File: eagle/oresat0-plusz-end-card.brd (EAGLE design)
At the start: 99.8 x 94.6 mm, 36 parts, among them J1 Harwin M55-7101242R, J10 R107064070_CONTACT, J11 R107064070_CONTACT, J12 R107064070_CONTACT, J13 R107064070_CONTACT, J14 R107064070_CONTACT, J15 R107064070_CONTACT, J16 R107064070_CONTACT, J2 Harwin M55-7101242R, J3 Harwin M55-7101242R, J4 Harwin M55-7101242R, J6 J-SAMTEC-TFM-120-X1-XXX-D-RA, J7 R107064070_CONTACT, J8 R107064070_CONTACT, J9 R107064070_CONTACT, U1 QCN-19D+, U2 QCN-19D+, U3 QCN-19D+

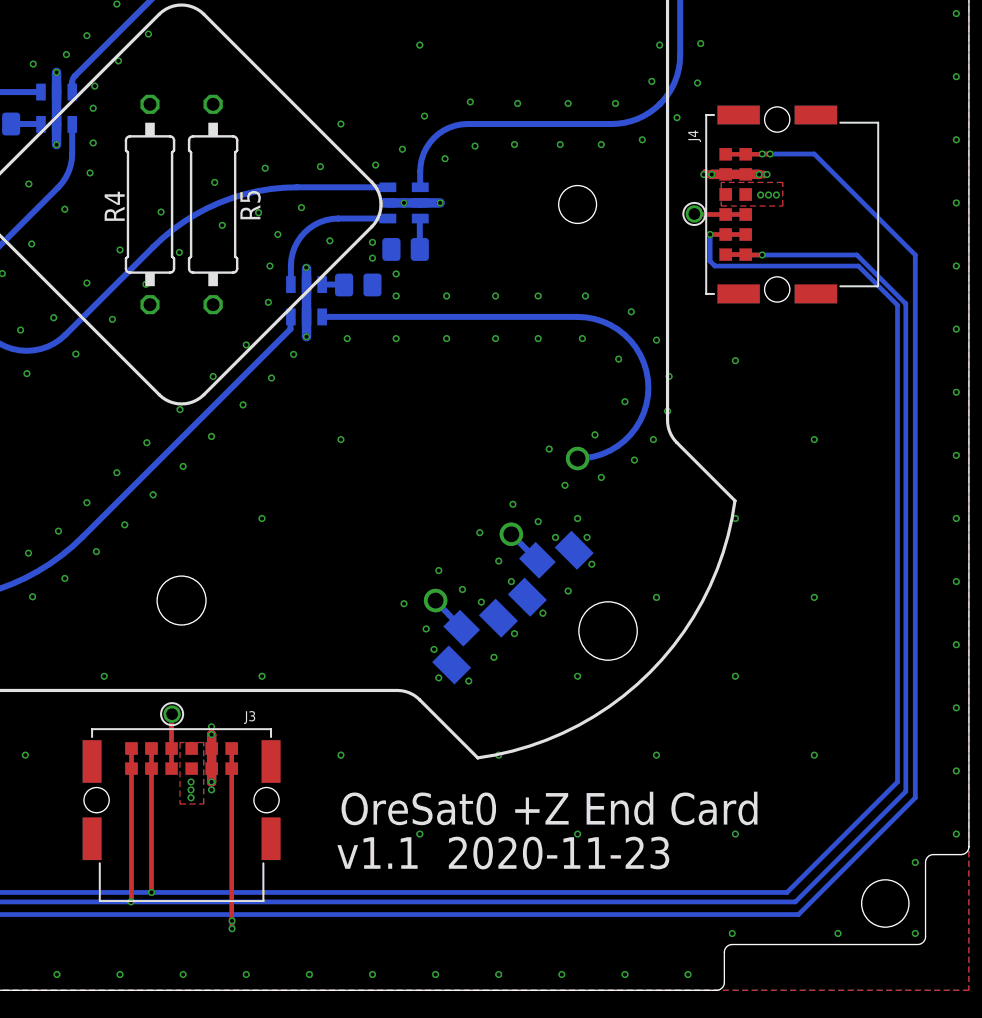
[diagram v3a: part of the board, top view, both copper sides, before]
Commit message: Small tweaks; reduced mezanine board size. Added flight tags. Off to fab!
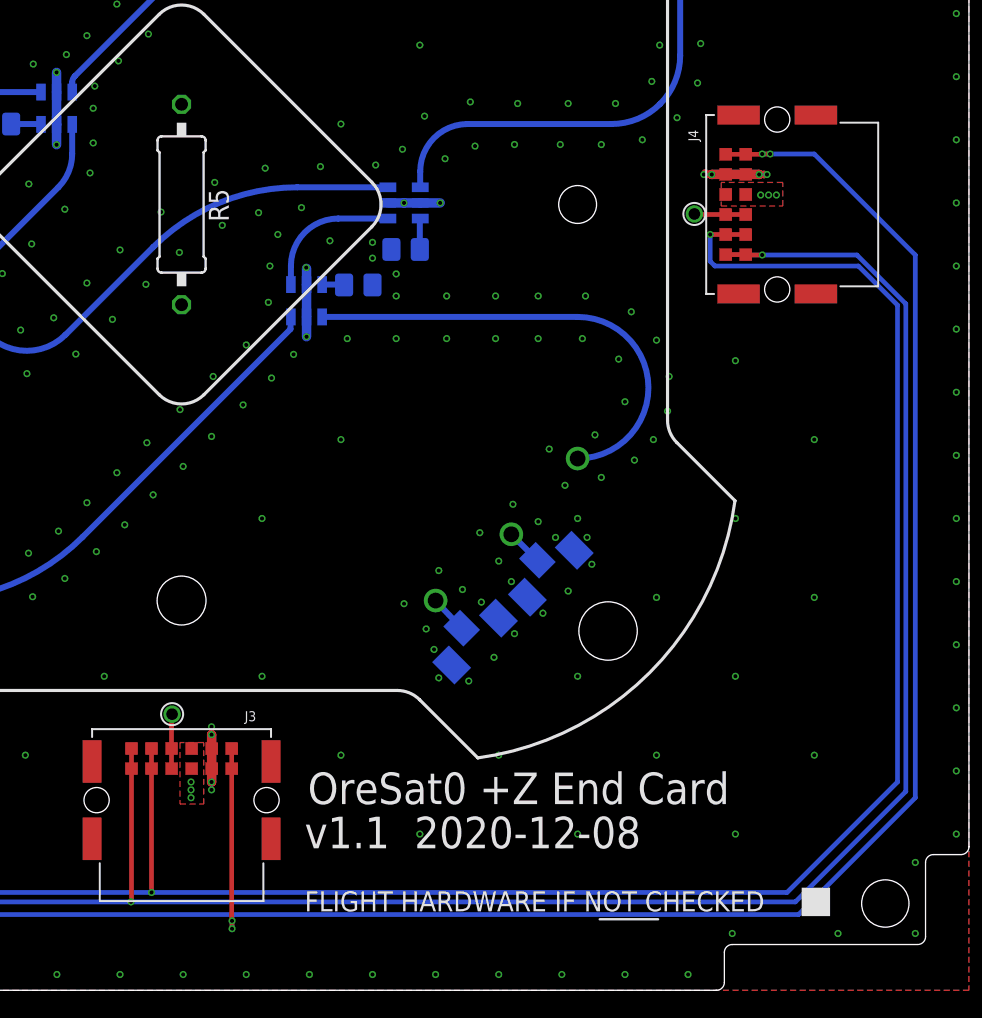
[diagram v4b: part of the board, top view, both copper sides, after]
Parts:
- removed R4: 1 1W, oresat-rcl:0309/12
- added U$1: FLIGHMARKERNEW, oresat-flight-marker:FLIGHTMARKER_NEW_BOARDS
- moved R5 2.00 mm to (49.9, 49.8)
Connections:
- net GND: no longer R4.1
- net TURNSTILE-DEPLOY: no longer R4.2
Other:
- board text added: "v1.1 2020-12-08"
- board text removed: "v1.1 2020-11-23"
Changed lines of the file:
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@@
 <layer number="14" name="Route14" color="22" fill="1" visible="no" active="no"/>
 <layer number="15" name="Route15" color="23" fill="1" visible="no" active="yes"/>
-<layer number="16" name="Bottom" color="1" fill="1" visible="no" active="yes"/>
+<layer number="16" name="Bottom" color="1" fill="1" visible="yes" active="yes"/>
 <layer number="17" name="Pads" color="2" fill="1" visible="yes" active="yes"/>
 <layer number="18" name="Vias" color="2" fill="1" visible="yes" active="yes"/>
@@
 <layer number="20" name="Dimension" color="24" fill="1" visible="yes" active="yes"/>
 <layer number="21" name="tPlace" color="7" fill="1" visible="yes" active="yes"/>
-<layer number="22" name="bPlace" color="7" fill="1" visible="no" active="yes"/>
+<layer number="22" name="bPlace" color="7" fill="1" visible="yes" active="yes"/>
 <layer number="23" name="tOrigins" color="15" fill="1" visible="yes" active="yes"/>
-<layer number="24" name="bOrigins" color="15" fill="1" visible="no" active="yes"/>
+<layer number="24" name="bOrigins" color="15" fill="1" visible="yes" active="yes"/>
 <layer number="25" name="tNames" color="7" fill="1" visible="yes" active="yes"/>
-<layer number="26" name="bNames" color="7" fill="1" visible="no" active="yes"/>
+<layer number="26" name="bNames" color="7" fill="1" visible="yes" active="yes"/>
 <layer number="27" name="tValues" color="7" fill="1" visible="no" active="yes"/>
 <layer number="28" name="bValues" color="7" fill="1" visible="no" active="yes"/>
 <layer number="29" name="tStop" color="7" fill="3" visible="yes" active="yes"/>
-<layer number="30" name="bStop" color="7" fill="6" visible="no" active="yes"/>
+<layer number="30" name="bStop" color="7" fill="6" visible="yes" active="yes"/>
 <layer number="31" name="tCream" color="7" fill="4" visible="no" active="yes"/>
 <layer number="32" name="bCream" color="7" fill="5" visible="no" active="yes"/>
@@
 <wire x1="60.01" y1="42.675" x2="75" y2="42.675" width="1.18" layer="30"/>
 <wire x1="75" y1="42.675" x2="76.5" y2="34" width="1.18" layer="30" curve="-159"/>
-<text x="59.9" y="10.5" size="2" layer="21" font="vector" ratio="10">OreSat0 +Z End Card</text>
-<text x="59.7" y="7.7" size="2" layer="21" font="vector" ratio="10">v1.1  2020-11-23</text>
+<text x="57.9" y="11.8" size="2" layer="21" font="vector" ratio="10">OreSat0 +Z End Card</text>
+<text x="57.7" y="9" size="2" layer="21" font="vector" ratio="10">v1.1  2020-12-08</text>
 <hole x="49.9" y="74.9" drill="3.1"/>
 <circle x="49.9" y="74.9" radius="3" width="0" layer="42"/>
@@
 <attribute name="VALUE" x="36.7" y="56.7" size="0.8" layer="28" font="vector" ratio="15" rot="MR180"/>
 </element>
-<element name="R4" library="oresat-rcl" package="0309/12" value="1 1W" x="47.9" y="49.8" smashed="yes" rot="R90">
-<attribute name="NAME" x="46.295003125" y="48.609" size="1.27" layer="25" ratio="10" rot="R90"/>
-<attribute name="VALUE" x="48.585803125" y="46.625" size="1.27" layer="27" ratio="10" rot="R90"/>
-</element>
-<element name="R5" library="oresat-rcl" package="0309/12" value="1 1W" x="51.9" y="49.8" smashed="yes" rot="R90">
-<attribute name="NAME" x="54.894996875" y="48.709" size="1.27" layer="25" ratio="10" rot="R90"/>
-<attribute name="VALUE" x="52.5858" y="46.625" size="1.27" layer="27" ratio="10" rot="R90"/>
+<element name="R5" library="oresat-rcl" package="0309/12" value="1 1W" x="49.9" y="49.8" locked="yes" smashed="yes" rot="R90">
+<attribute name="NAME" x="52.894996875" y="48.709" locked="yes" size="1.27" layer="25" ratio="10" rot="R90"/>
+<attribute name="VALUE" x="50.5858" y="46.625" locked="yes" size="1.27" layer="27" ratio="10" rot="R90"/>
 </element>
 <element name="J7" library="J-Radiall-R107064070-RF" package="R107064070_CONTACT" value="R107064070_CONTACT" x="88" y="75.9" locked="yes" smashed="yes" rot="MR90">
@@
 <attribute name="VALUE" x="68.5" y="19.271571875" locked="yes" size="0.655" layer="28" font="vector" ratio="20" rot="MR135"/>
 </element>
+<element name="U$1" library="oresat-flight-marker" package="FLIGHTMARKER_NEW_BOARDS" value="FLIGHMARKERNEW" x="57.7" y="5" smashed="yes"/>
 </elements>
 <signals>
@@
 <via x="30" y="44.9" extent="1-16" drill="0.254"/>
 <via x="65" y="89.9" extent="1-16" drill="0.254"/>
-<contactref element="R4" pad="1"/>
 <contactref element="R5" pad="1"/>
 <contactref element="J7" pad="P$3"/>
@@
 <contactref element="J6" pad="10"/>
 <contactref element="R5" pad="2"/>
-<contactref element="R4" pad="2"/>
 <polygon width="0.127" layer="2" isolate="0.2" thermals="no">
 <vertex x="33.8" y="90.5"/>
 <vertex x="33.8" y="54.5"/>
-<vertex x="54.4" y="54.5"/>
-<vertex x="54.4" y="65.2"/>
+<vertex x="51.6" y="54.5"/>
+<vertex x="51.6" y="68"/>
 <vertex x="42.5" y="77.1"/>
 <vertex x="42.5" y="90.5"/>

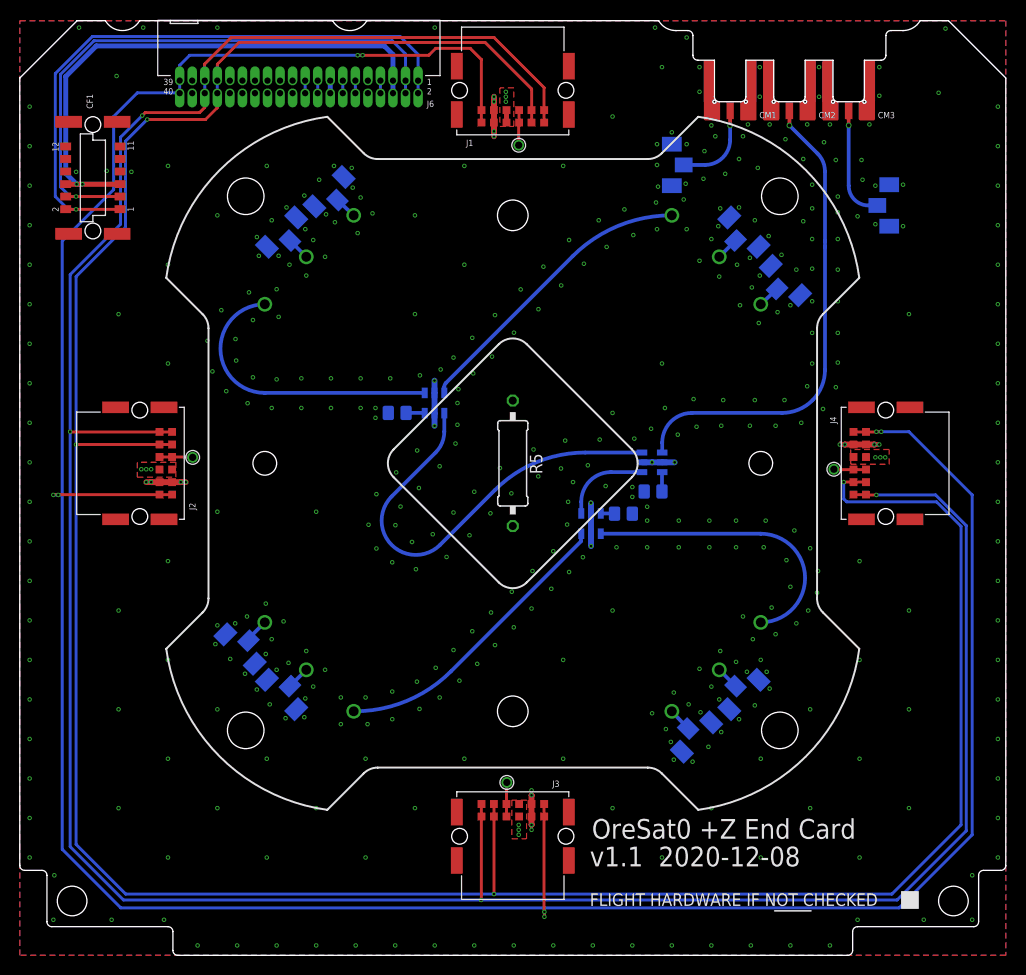
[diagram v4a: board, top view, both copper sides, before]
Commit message: Version 1.2 of the OreSat0 end card and mezzanine.
Largest change is the position of the antennas on the end card; changes to the deployer changed the antenna placement which triggered everything else.

Other changes include fiducials, attributes cleanup, move to 0603 resistors, and misc polish.
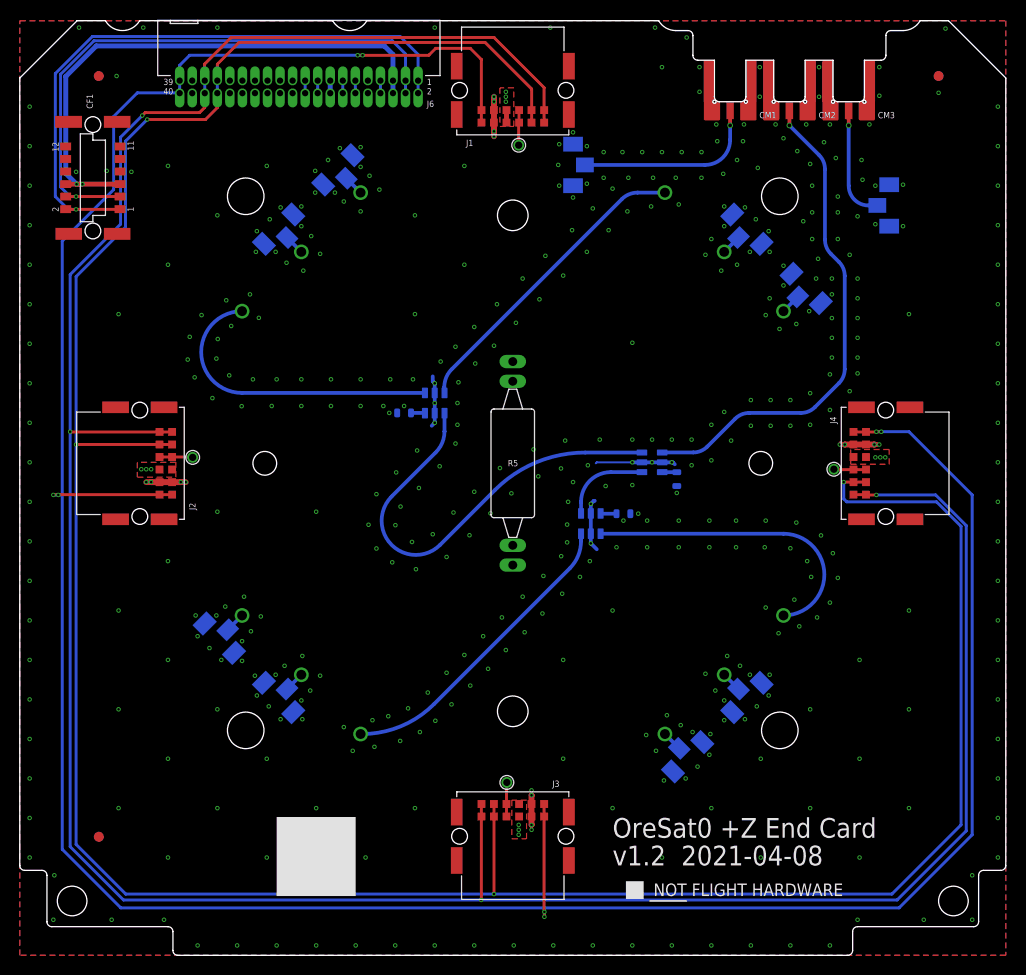
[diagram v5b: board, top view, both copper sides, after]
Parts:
- added FIDUCIAL1, FIDUCIAL2, FIDUCIAL3, FIDUCIAL4, FIDUCIAL5, FIDUCIAL6: FIDUCIAL-1.0X2.0, monitor-v2-debug:FIDUCIAL-1.0X2.0
- R1, R2, R3: device oresat-rcl:.0805-B-NOSILK -> oresat-rcl:.0603-C-NOSILK
- R5: value 1 1W -> 7.5 1W; device oresat-rcl:0309/12 -> R-Vishay-PAC1000-1W-resistor:PAC100-FOR-MELTWIRE
- U1, U2, U3: value QCN-19D+ -> QCN-19+; device Mini-Circuits-QCN-19D+_Phase-shifter:QVN-19D+ -> U-MiniCirc-QCN-XXX+-quad:QCN-XXX+
- moved U2 20.0 mm to (57.8, 43.7), turned to 180 degrees
- moved U3 20.0 mm to (42.0, 55.9), turned to 0 degrees
- moved J12 10.0 mm to (56.0, 80.0)
- moved U$1 4.03 mm to (61.6, 6.00)
- moved R1 2.71 mm to (66.5, 48.2), turned to 90 degrees
- moved J14 2.38 mm to (32.2, 79.5)
- moved J15 2.37 mm to (20.2, 32.1)
- moved J13 2.25 mm to (79.6, 67.5)
- moved J16 2.19 mm to (67.6, 20.1)
- moved R3 0.70 mm to (38.9, 54.9)
- moved J10 0.42 mm to (26.2, 73.5)
- moved J9 0.42 mm to (26.2, 26.1)
- moved J11 0.42 mm to (73.6, 73.5)
- moved J8 0.42 mm to (73.6, 26.1)
- turned R5 to 180 degrees
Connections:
- net GND: now also R5.P$1, R5.P$2, U1.2, U1.5, U2.2, U2.5, U3.2, U3.5; no longer R5.1, U1.P$2, U1.P$5, U2.P$2, U2.P$5, U3.P$2, U3.P$5
- net LBAND: now also U1.1; no longer U1.P$1
- net LBAND-1/4L: now also U1.6, U3.1; no longer U1.P$6, U2.P$1
- net LBAND-SHORT: now also U1.4, U2.1; no longer U1.P$4, U3.P$1
- net LBAND_0: now also U2.4; no longer U3.P$4
- net LBAND_180: now also U3.4; no longer U2.P$4
- net LBAND_270: now also U3.6; no longer U2.P$6
- net LBAND_90: now also U2.6; no longer U3.P$6
- net N$3: now also U1.3; no longer U1.P$3
- net N$4: now also U2.3; no longer U3.P$3
- net N$6: now also U3.3; no longer U2.P$3
- net TURNSTILE-DEPLOY: now also R5.P$3, R5.P$4; no longer R5.2
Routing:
- net SBAND: track 8.73 -> 18.7 mm
- net GND: track 26.4 -> 32.9 mm, vias 427 -> 454
- net LBAND_0: track 25.2 -> 26.8 mm
- net LBAND_180: track 25.2 -> 26.8 mm
- net LBAND: track 48.6 -> 50.1 mm
- net LBAND_270: track 30.0 -> 31.4 mm
- net LBAND_90: track 30.0 -> 31.2 mm
- net SBAND_90: track 2.56 -> 2.05 mm
- net N$3: track 1.98 -> 1.48 mm
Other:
- board text added: "v1.2 2021-04-08"
- board text removed: "v1.1 2020-12-08"

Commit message: Fixed bad part number for end card to end cap connector.
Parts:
- CF1: value J-HARWIN-M55-60X1242R -> J-HARWIN-M55-6001242R
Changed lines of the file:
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@@
 <grid distance="0.1" unitdist="mm" unit="mm" style="lines" multiple="1" display="yes" altdistance="0.1" altunitdist="mm" altunit="mm"/>
 <layers>
-<layer number="1" name="Top" color="4" fill="1" visible="no" active="yes"/>
+<layer number="1" name="Top" color="4" fill="1" visible="yes" active="yes"/>
 <layer number="2" name="Route2" color="16" fill="1" visible="no" active="yes"/>
 <layer number="3" name="Route3" color="17" fill="1" visible="no" active="no"/>
@@
 <layer number="14" name="Route14" color="22" fill="1" visible="no" active="no"/>
 <layer number="15" name="Route15" color="23" fill="1" visible="no" active="yes"/>
-<layer number="16" name="Bottom" color="1" fill="1" visible="yes" active="yes"/>
+<layer number="16" name="Bottom" color="1" fill="1" visible="no" active="yes"/>
 <layer number="17" name="Pads" color="2" fill="1" visible="yes" active="yes"/>
 <layer number="18" name="Vias" color="2" fill="1" visible="yes" active="yes"/>
 <layer number="19" name="Unrouted" color="6" fill="1" visible="yes" active="yes"/>
 <layer number="20" name="Dimension" color="24" fill="1" visible="yes" active="yes"/>
-<layer number="21" name="tPlace" color="7" fill="1" visible="no" active="yes"/>
-<layer number="22" name="bPlace" color="7" fill="1" visible="yes" active="yes"/>
-<layer number="23" name="tOrigins" color="15" fill="1" visible="no" active="yes"/>
-<layer number="24" name="bOrigins" color="15" fill="1" visible="yes" active="yes"/>
+<layer number="21" name="tPlace" color="7" fill="1" visible="yes" active="yes"/>
+<layer number="22" name="bPlace" color="7" fill="1" visible="no" active="yes"/>
+<layer number="23" name="tOrigins" color="15" fill="1" visible="yes" active="yes"/>
+<layer number="24" name="bOrigins" color="15" fill="1" visible="no" active="yes"/>
 <layer number="25" name="tNames" color="7" fill="1" visible="no" active="yes"/>
 <layer number="26" name="bNames" color="7" fill="1" visible="no" active="yes"/>
@@
 <layer number="28" name="bValues" color="7" fill="1" visible="no" active="yes"/>
 <layer number="29" name="tStop" color="7" fill="3" visible="no" active="yes"/>
-<layer number="30" name="bStop" color="7" fill="6" visible="yes" active="yes"/>
+<layer number="30" name="bStop" color="7" fill="6" visible="no" active="yes"/>
 <layer number="31" name="tCream" color="7" fill="4" visible="no" active="yes"/>
 <layer number="32" name="bCream" color="7" fill="5" visible="no" active="yes"/>
@@
 <layer number="38" name="bTest" color="7" fill="1" visible="no" active="yes"/>
 <layer number="39" name="tKeepout" color="4" fill="11" visible="no" active="yes"/>
-<layer number="40" name="bKeepout" color="1" fill="11" visible="yes" active="yes"/>
+<layer number="40" name="bKeepout" color="1" fill="11" visible="no" active="yes"/>
 <layer number="41" name="tRestrict" color="4" fill="10" visible="no" active="yes"/>
 <layer number="42" name="bRestrict" color="1" fill="10" visible="no" active="yes"/>
@@
 <layer number="49" name="Reference" color="7" fill="1" visible="no" active="yes"/>
 <layer number="50" name="dxf" color="11" fill="1" visible="no" active="yes"/>
-<layer number="51" name="tDocu" color="7" fill="1" visible="no" active="yes"/>
-<layer number="52" name="bDocu" color="7" fill="1" visible="yes" active="yes"/>
+<layer number="51" name="tDocu" color="7" fill="1" visible="yes" active="yes"/>
+<layer number="52" name="bDocu" color="7" fill="1" visible="no" active="yes"/>
 <layer number="53" name="tGND_GNDA" color="7" fill="9" visible="no" active="no"/>
 <layer number="54" name="bGND_GNDA" color="1" fill="9" visible="no" active="no"/>
@@
 <attribute name="P-NP" value="P" x="87.65" y="49.8" locked="yes" size="1.778" layer="27" rot="R90" display="off"/>
 </element>
-<element name="CF1" library="J-Harwin-M55-60X1242R-12pin-1.27mm-F-vertical" package="HARWIN-M55-60X1242R" value="J-HARWIN-M55-60X1242R" x="7.4" y="78.7" locked="yes" smashed="yes" rot="R90">
-<attribute name="DESCRIPTION" value="connector" x="7.4" y="78.7" locked="yes" size="1.778" layer="27" rot="R90" display="off"/>
-<attribute name="DIST" value="Digi-Key" x="7.4" y="78.7" locked="yes" size="1.778" layer="27" rot="R90" display="off"/>
-<attribute name="DIST_PN" value="952-3851-1-ND" x="7.4" y="78.7" locked="yes" size="1.778" layer="27" rot="R90" display="off"/>
-<attribute name="GENERIC" value="N" x="7.4" y="78.7" locked="yes" size="1.778" layer="27" rot="R90" display="off"/>
+<element name="CF1" library="J-Harwin-M55-60X1242R-12pin-1.27mm-F-vertical" package="HARWIN-M55-60X1242R" value="J-HARWIN-M55-6001242R" x="7.4" y="78.7" locked="yes" smashed="yes" rot="R90">
 <attribute name="MFG" value="Harwin" x="7.4" y="78.7" locked="yes" size="1.778" layer="27" rot="R90" display="off"/>
-<attribute name="MFG_PN" value="M55-6021242R" x="7.4" y="78.7" locked="yes" size="1.778" layer="27" rot="R90" display="off"/>
+<attribute name="MFG_PN" value="M55-60X1242R" x="7.4" y="78.7" locked="yes" size="1.778" layer="27" rot="R90" display="off"/>
 <attribute name="NAME" x="7.4" y="85.685" locked="yes" size="0.635" layer="25" font="vector" ratio="20" rot="R90"/>
 <attribute name="P-NP" value="P" x="7.4" y="78.7" locked="yes" size="1.778" layer="27" rot="R90" display="off"/>
